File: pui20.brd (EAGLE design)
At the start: 160 x 100 mm, 0 parts

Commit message: + pui.sch (beginning)
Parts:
- added ANSCHLUSS1:X1: WANNENSTECKER-16, iceberg20:2X8
- added AUSGABE1:LED1, AUSGABE1:LED2: WS2812B, iceberg20:5050
- added AUSGABE1:LED10, AUSGABE1:LED3, AUSGABE1:LED4, AUSGABE1:LED5, AUSGABE1:LED6, AUSGABE1:LED7, AUSGABE1:LED8, AUSGABE1:LED9: LED-GREEN1, iceberg20:1206
- added AUSGABE1:R1, AUSGABE1:R2, AUSGABE1:R3, AUSGABE1:R4: 330, iceberg20:R0805
- added EINGABE1:S1, EINGABE1:S2, EINGABE1:S3, EINGABE1:S6: SMD-BUTTON, iceberg20:SWITCH-6MM-SMD
- added EINGABE1:S4, EINGABE1:S5: BUTTON-12MM, iceberg20:SWITCH-12MM-THT
- added EINGABE1:S7, EINGABE1:S8, EINGABE1:S9: TOGGLE-SWITCH, iceberg20:TOGGLE-SWITCH
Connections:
- new net +12V: ANSCHLUSS1:X1.1
- new net +5V: ANSCHLUSS1:X1.2
- new net ANSCHLUSS1:INTERRUPT: ANSCHLUSS1:X1.16
- new net ANSCHLUSS1:SCL: ANSCHLUSS1:X1.4
- new net ANSCHLUSS1:SDA: ANSCHLUSS1:X1.6
- new net AUSGABE1:+5V: AUSGABE1:LED1.VDD, AUSGABE1:LED2.VDD
- new net AUSGABE1:GND: AUSGABE1:LED1.GND, AUSGABE1:LED10.C, AUSGABE1:LED2.GND, AUSGABE1:LED6.C, AUSGABE1:LED7.C, AUSGABE1:LED8.C
- new net AUSGABE1:N$1: AUSGABE1:LED3.C, AUSGABE1:LED6.A
- new net AUSGABE1:N$11: AUSGABE1:LED9.A, AUSGABE1:R4.2
- new net AUSGABE1:N$12: AUSGABE1:LED10.A, AUSGABE1:LED9.C
- new net AUSGABE1:N$2: AUSGABE1:LED3.A, AUSGABE1:R1.2
- new net AUSGABE1:N$3: AUSGABE1:LED4.C, AUSGABE1:LED7.A
- new net AUSGABE1:N$4: AUSGABE1:LED5.C, AUSGABE1:LED8.A
- new net AUSGABE1:N$5: AUSGABE1:LED1.OUT, AUSGABE1:LED2.IN
- new net AUSGABE1:N$6: AUSGABE1:LED4.A, AUSGABE1:R2.2
- new net AUSGABE1:N$7: AUSGABE1:LED5.A, AUSGABE1:R3.2
- new net AUSGABE1:SHIFT-LED: AUSGABE1:R4.1
- new net EINGABE1:CALIBRATION-B: EINGABE1:S3.A1, EINGABE1:S3.A2
- new net EINGABE1:GND: EINGABE1:S1.B1, EINGABE1:S1.B2, EINGABE1:S2.B1, EINGABE1:S2.B2, EINGABE1:S3.B1, EINGABE1:S3.B2, EINGABE1:S4.3, EINGABE1:S5.3, EINGABE1:S6.B1, EINGABE1:S6.B2, EINGABE1:S7.C, EINGABE1:S8.C, EINGABE1:S9.C
- new net EINGABE1:KICK-B: EINGABE1:S2.A1, EINGABE1:S2.A2
- new net EINGABE1:SHIFT-B: EINGABE1:S6.A1, EINGABE1:S6.A2
- new net N$1: ANSCHLUSS1:X1.3, ANSCHLUSS1:X1.5, ANSCHLUSS1:X1.7
- new net N$2: ANSCHLUSS1:X1.8, EINGABE1:S4.1
- new net N$3: ANSCHLUSS1:X1.9, EINGABE1:S5.1
- new net N$4: ANSCHLUSS1:X1.15, EINGABE1:S1.A1, EINGABE1:S1.A2
- new net N$5: ANSCHLUSS1:X1.14, AUSGABE1:LED1.IN
- new net N$6: AUSGABE1:R3.1, EINGABE1:S9.A
- new net N$7: AUSGABE1:R1.1, EINGABE1:S7.A
- new net N$8: AUSGABE1:R2.1, EINGABE1:S8.A

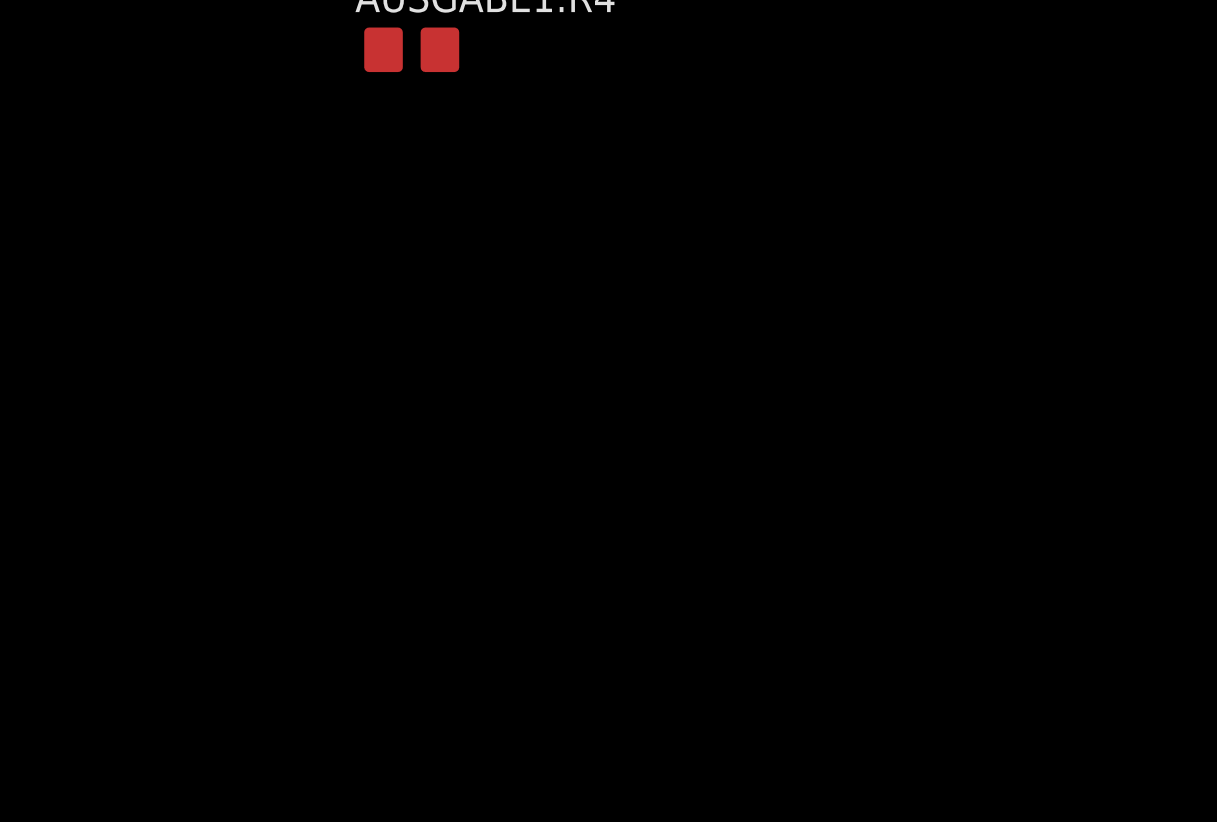
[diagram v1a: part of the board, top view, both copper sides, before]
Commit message: - pui.sch (Eingabe + Ausgabe)
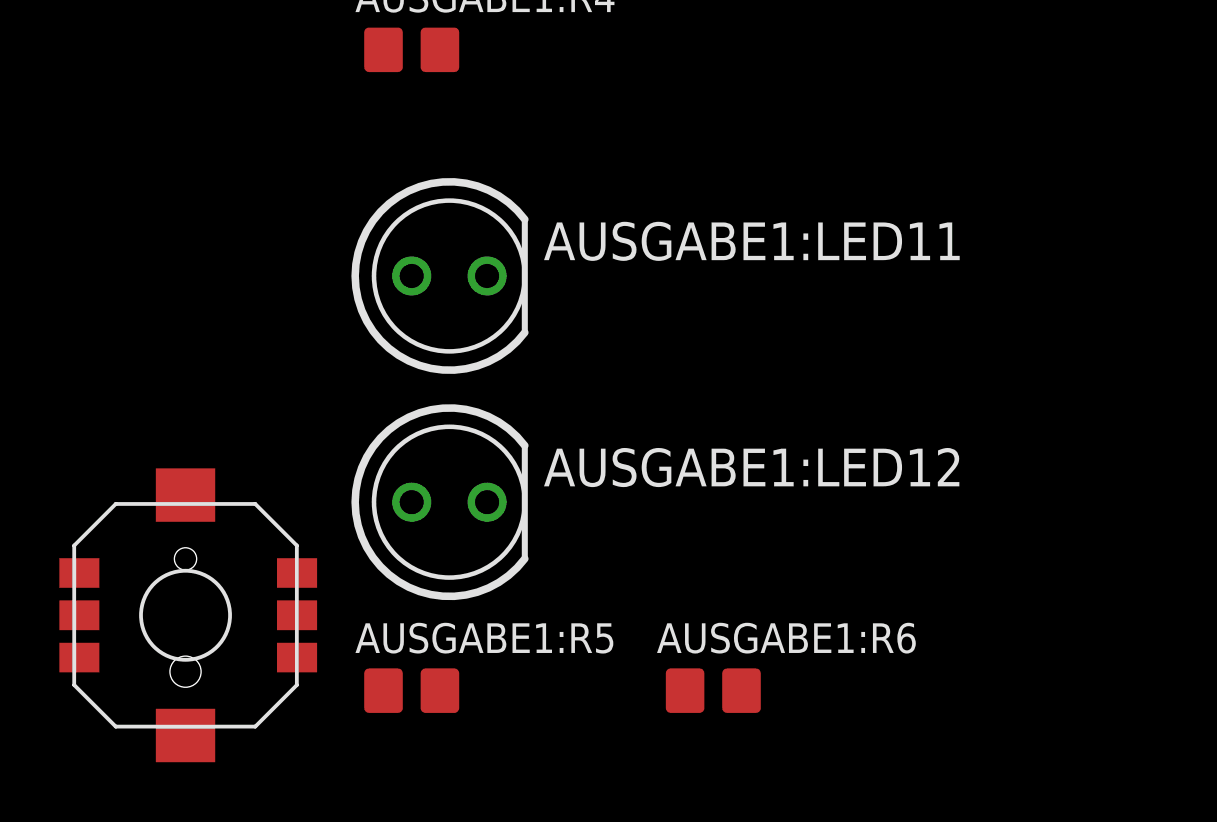
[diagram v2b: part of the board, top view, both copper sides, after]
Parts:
- added AUSGABE1:LED11, AUSGABE1:LED12: LED-GREEN-THT, iceberg20:LED_LED5MM
- added AUSGABE1:R5, AUSGABE1:R6: R, iceberg20:R0805
- added EINGABE1:U$1: JOYSTICK, iceberg20:SKRHAAE010
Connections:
- new net AUSGABE1:DEFENCE-LED: AUSGABE1:R6.1
- new net AUSGABE1:N$8: AUSGABE1:LED11.A, AUSGABE1:R5.2
- new net AUSGABE1:N$9: AUSGABE1:LED12.A, AUSGABE1:R6.2
- new net AUSGABE1:STRIKER-LED: AUSGABE1:R5.1
- new net EINGABE1:CENTER-J: EINGABE1:U$1.CENTER
- new net EINGABE1:DOWN-J: EINGABE1:U$1.C
- new net EINGABE1:LEFT-J: EINGABE1:U$1.A
- new net EINGABE1:RIGHT-J: EINGABE1:U$1.D
- new net EINGABE1:UP-J: EINGABE1:U$1.B
- net AUSGABE1:GND: now also AUSGABE1:LED11.K, AUSGABE1:LED12.K
- net EINGABE1:GND: now also EINGABE1:U$1.COMMON
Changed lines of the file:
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@@
 <attribute name="VALUE" x="-76.835" y="-106.68" size="1" layer="27" font="vector" ratio="20"/>
+</element>
+<element name="AUSGABE1:LED11" library="iceberg20" package="LED_LED5MM" value="LED-GREEN-THT" x="-73.66" y="-111.76" smashed="yes">
+<attribute name="BESTAND" value="" x="-73.66" y="-110.49" size="1.778" layer="27" display="off"/>
+<attribute name="HERSTELLER" value="" x="-73.66" y="-110.49" size="1.778" layer="27" display="off"/>
+<attribute name="HERSTELLER-NR" value="" x="-73.66" y="-110.49" size="1.778" layer="27" display="off"/>
+<attribute name="NAME" x="-70.485" y="-111.2266" size="1.27" layer="25" font="vector" ratio="20"/>
+<attribute name="SUPPLIER" value="" x="-73.66" y="-110.49" size="1.778" layer="27" display="off"/>
+<attribute name="SUPPLIER-NR" value="" x="-73.66" y="-110.49" size="1.778" layer="27" display="off"/>
+<attribute name="VALUE" x="-70.4596" y="-113.5634" size="1.27" layer="27" font="vector" ratio="20"/>
+</element>
+<element name="AUSGABE1:LED12" library="iceberg20" package="LED_LED5MM" value="LED-GREEN-THT" x="-73.66" y="-119.38" smashed="yes">
+<attribute name="BESTAND" value="" x="-73.66" y="-118.11" size="1.778" layer="27" display="off"/>
+<attribute name="HERSTELLER" value="" x="-73.66" y="-118.11" size="1.778" layer="27" display="off"/>
+<attribute name="HERSTELLER-NR" value="" x="-73.66" y="-118.11" size="1.778" layer="27" display="off"/>
+<attribute name="NAME" x="-70.485" y="-118.8466" size="1.27" layer="25" font="vector" ratio="20"/>
+<attribute name="SUPPLIER" value="" x="-73.66" y="-118.11" size="1.778" layer="27" display="off"/>
+<attribute name="SUPPLIER-NR" value="" x="-73.66" y="-118.11" size="1.778" layer="27" display="off"/>
+<attribute name="VALUE" x="-70.4596" y="-121.1834" size="1.27" layer="27" font="vector" ratio="20"/>
+</element>
+<element name="AUSGABE1:R5" library="iceberg20" package="R0805" package3d_urn="urn:adsk.eagle:package:23553/2" value="R" x="-74.93" y="-125.73" smashed="yes">
+<attribute name="BESTAND" value="-" x="-74.93" y="-124.46" size="1.778" layer="27" display="off"/>
+<attribute name="HERSTELLER" value="-" x="-74.93" y="-124.46" size="1.778" layer="27" display="off"/>
+<attribute name="HERSTELLER-NR" value="-" x="-74.93" y="-124.46" size="1.778" layer="27" display="off"/>
+<attribute name="NAME" x="-76.835" y="-124.46" size="1" layer="25" font="vector" ratio="20"/>
+<attribute name="SUPPLIER" value="-" x="-74.93" y="-124.46" size="1.778" layer="27" display="off"/>
+<attribute name="SUPPLIER-NR" value="-" x="-74.93" y="-124.46" size="1.778" layer="27" display="off"/>
+<attribute name="TOLERANZ" value="5%" x="-74.93" y="-124.46" size="1.778" layer="27" display="off"/>
+<attribute name="VALUE" x="-76.835" y="-128.27" size="1" layer="27" font="vector" ratio="20"/>
+</element>
+<element name="AUSGABE1:R6" library="iceberg20" package="R0805" package3d_urn="urn:adsk.eagle:package:23553/2" value="R" x="-64.77" y="-125.73" smashed="yes">
+<attribute name="BESTAND" value="-" x="-74.93" y="-130.81" size="1.778" layer="27" display="off"/>
+<attribute name="HERSTELLER" value="-" x="-74.93" y="-130.81" size="1.778" layer="27" display="off"/>
+<attribute name="HERSTELLER-NR" value="-" x="-74.93" y="-130.81" size="1.778" layer="27" display="off"/>
+<attribute name="NAME" x="-66.675" y="-124.46" size="1" layer="25" font="vector" ratio="20"/>
+<attribute name="SUPPLIER" value="-" x="-74.93" y="-130.81" size="1.778" layer="27" display="off"/>
+<attribute name="SUPPLIER-NR" value="-" x="-74.93" y="-130.81" size="1.778" layer="27" display="off"/>
+<attribute name="TOLERANZ" value="5%" x="-74.93" y="-130.81" size="1.778" layer="27" display="off"/>
+<attribute name="VALUE" x="-66.675" y="-128.27" size="1" layer="27" font="vector" ratio="20"/>
+</element>
+<element name="EINGABE1:U$1" library="iceberg20" package="SKRHAAE010" value="JOYSTICK" x="-82.55" y="-123.19" smashed="yes">
+<attribute name="BESTAND" value="0" x="-82.55" y="-123.19" size="1.778" layer="27" display="off"/>
+<attribute name="HERSTELLER" value="ALPS" x="-82.55" y="-123.19" size="1.778" layer="27" display="off"/>
+<attribute name="HERSTELLER-NR" value="SKRHAAE010 " x="-82.55" y="-123.19" size="1.778" layer="27" display="off"/>
+<attribute name="SUPPLIER" value="Mouser" x="-82.55" y="-123.19" size="1.778" layer="27" display="off"/>
+<attribute name="SUPPLIER-NR" value="688-SKRHAAE010 " x="-82.55" y="-123.19" size="1.778" layer="27" display="off"/>
 </element>
 </elements>
@@
 <contactref element="EINGABE1:S9" pad="C"/>
 <contactref element="EINGABE1:S8" pad="C"/>
+<contactref element="EINGABE1:U$1" pad="COMMON"/>
+<wire x1="5.08" y1="-80.01" x2="-78.793" y2="-123.19" width="0" layer="19" extent="1-1"/>
 <wire x1="5.08" y1="-76.2" x2="5.08" y2="-80.01" width="0" layer="19" extent="1-1"/>
 <wire x1="5.08" y1="-72.39" x2="5.08" y2="-76.2" width="0" layer="19" extent="1-1"/>
@@
 <contactref element="AUSGABE1:LED7" pad="C"/>
 <contactref element="AUSGABE1:LED10" pad="C"/>
+<contactref element="AUSGABE1:LED11" pad="K"/>
+<contactref element="AUSGABE1:LED12" pad="K"/>
+<wire x1="-72.39" y1="-111.76" x2="-72.39" y2="-119.38" width="0" layer="19" extent="1-1"/>
+<wire x1="-67.08" y1="-77.47" x2="-72.39" y2="-111.76" width="0" layer="19" extent="1-1"/>
 <wire x1="-60.73" y1="-77.47" x2="-67.08" y2="-77.47" width="0" layer="19" extent="1-1"/>
 <wire x1="-54.38" y1="-77.47" x2="-60.73" y2="-77.47" width="0" layer="19" extent="1-1"/>
@@
 <wire x1="2.54" y1="-76.2" x2="-75.88" y2="-91.44" width="0" layer="19" extent="1-1"/>
 </signal>
+<signal name="AUSGABE1:N$8">
+<contactref element="AUSGABE1:LED11" pad="A"/>
+<contactref element="AUSGABE1:R5" pad="2"/>
+<wire x1="-74.93" y1="-111.76" x2="-73.98" y2="-125.73" width="0" layer="19" extent="1-1"/>
+</signal>
+<signal name="AUSGABE1:N$9">
+<contactref element="AUSGABE1:LED12" pad="A"/>
+<contactref element="AUSGABE1:R6" pad="2"/>
+<wire x1="-63.82" y1="-125.73" x2="-74.93" y2="-119.38" width="0" layer="19" extent="1-1"/>
+</signal>
+<signal name="AUSGABE1:STRIKER-LED">
+<contactref element="AUSGABE1:R5" pad="1"/>
+</signal>
+<signal name="AUSGABE1:DEFENCE-LED">
+<contactref element="AUSGABE1:R6" pad="1"/>
+</signal>
+<signal name="EINGABE1:LEFT-J">
+<contactref element="EINGABE1:U$1" pad="A"/>
+</signal>
+<signal name="EINGABE1:CENTER-J">
+<contactref element="EINGABE1:U$1" pad="CENTER"/>
+</signal>
+<signal name="EINGABE1:DOWN-J">
+<contactref element="EINGABE1:U$1" pad="C"/>
+</signal>
+<signal name="EINGABE1:UP-J">
+<contactref element="EINGABE1:U$1" pad="B"/>
+</signal>
+<signal name="EINGABE1:RIGHT-J">
+<contactref element="EINGABE1:U$1" pad="D"/>
+</signal>
 </signals>

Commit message: + pui.brd (begin routing)
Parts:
- added EXPANDER1:C1: 200nF, iceberg20:C0805
- added EXPANDER1:IC1: GPIO-EXPANDER, iceberg20:DIL28-3
- added EXPANDER1:R1: 1k, iceberg20:R0805
- moved AUSGABE1:R6 214.9 mm to (70.5, 41.3), turned to 270 degrees
- moved EINGABE1:U$1 208.4 mm to (80.7, 6.36)
- moved AUSGABE1:R4 201.7 mm to (50.9, 53.4), turned to 90 degrees
- moved AUSGABE1:R5 196.1 mm to (31.7, 38.8), turned to 270 degrees
- moved AUSGABE1:R1 189.2 mm to (53.9, 53.4), turned to 90 degrees
- moved AUSGABE1:LED8 184.0 mm to (89.7, 16.3)
- moved AUSGABE1:R3 181.1 mm to (41.4, 40.9)
- moved AUSGABE1:LED7 180.5 mm to (89.5, 20.3)
- moved AUSGABE1:R2 180.1 mm to (39.9, 47.3)
- moved AUSGABE1:LED12 179.8 mm to (46.3, 14.5)
- moved AUSGABE1:LED6 177.1 mm to (89.4, 23.8)
- moved AUSGABE1:LED11 168.5 mm to (37.8, 14.6)
- moved AUSGABE1:LED5 163.0 mm to (83.8, 16.3)
- moved AUSGABE1:LED4 160.1 mm to (83.6, 20.3)
- moved AUSGABE1:LED3 157.2 mm to (83.5, 23.8)
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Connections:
- removed net ANSCHLUSS1:SCL: ANSCHLUSS1:X1.4
- removed net ANSCHLUSS1:SDA: ANSCHLUSS1:X1.6
- removed net AUSGABE1:+5V: AUSGABE1:LED1.VDD, AUSGABE1:LED2.VDD
- removed net AUSGABE1:DEFENCE-LED: AUSGABE1:R6.1
- removed net AUSGABE1:GND: AUSGABE1:LED1.GND, AUSGABE1:LED10.C, AUSGABE1:LED11.K, AUSGABE1:LED12.K, AUSGABE1:LED2.GND, AUSGABE1:LED6.C, AUSGABE1:LED7.C, AUSGABE1:LED8.C
- removed net AUSGABE1:SHIFT-LED: AUSGABE1:R4.1
- removed net AUSGABE1:STRIKER-LED: AUSGABE1:R5.1
- removed net EINGABE1:CALIBRATION-B: EINGABE1:S3.A1, EINGABE1:S3.A2
- removed net EINGABE1:CENTER-J: EINGABE1:U$1.CENTER
- removed net EINGABE1:DOWN-J: EINGABE1:U$1.C
- removed net EINGABE1:GND: EINGABE1:S1.B1, EINGABE1:S1.B2, EINGABE1:S2.B1, EINGABE1:S2.B2, EINGABE1:S3.B1, EINGABE1:S3.B2, EINGABE1:S4.3, EINGABE1:S5.3, EINGABE1:S6.B1, EINGABE1:S6.B2, EINGABE1:S7.C, EINGABE1:S8.C, EINGABE1:S9.C, EINGABE1:U$1.COMMON
- removed net EINGABE1:KICK-B: EINGABE1:S2.A1, EINGABE1:S2.A2
- removed net EINGABE1:LEFT-J: EINGABE1:U$1.A
- removed net EINGABE1:RIGHT-J: EINGABE1:U$1.D
- removed net EINGABE1:SHIFT-B: EINGABE1:S6.A1, EINGABE1:S6.A2
- removed net EINGABE1:UP-J: EINGABE1:U$1.B
- removed net N$8: AUSGABE1:R2.1, EINGABE1:S8.A
- new net EXPANDER1:A0: EXPANDER1:IC1.15
- new net EXPANDER1:A1: EXPANDER1:IC1.16
- new net EXPANDER1:A2: EXPANDER1:IC1.17
- new net EXPANDER1:GPA5: EXPANDER1:IC1.26
- new net EXPANDER1:GPA6: EXPANDER1:IC1.27
- new net EXPANDER1:GPA7: EXPANDER1:IC1.28
- new net EXPANDER1:INTA: EXPANDER1:IC1.20
- new net EXPANDER1:INTB: EXPANDER1:IC1.19
- new net EXPANDER1:NC: EXPANDER1:IC1.11
- new net EXPANDER1:RESET: EXPANDER1:IC1.18, EXPANDER1:R1.1
- new net GND: AUSGABE1:LED1.GND, AUSGABE1:LED10.C, AUSGABE1:LED11.K, AUSGABE1:LED12.K, AUSGABE1:LED2.GND, AUSGABE1:LED6.C, AUSGABE1:LED7.C, AUSGABE1:LED8.C, EINGABE1:S1.B1, EINGABE1:S1.B2, EINGABE1:S2.B1, EINGABE1:S2.B2, EINGABE1:S3.B1, EINGABE1:S3.B2, EINGABE1:S4.3, EINGABE1:S5.3, EINGABE1:S6.B1, EINGABE1:S6.B2, EINGABE1:S7.C, EINGABE1:S8.C, EINGABE1:S9.C, EINGABE1:U$1.COMMON, EXPANDER1:C1.2, EXPANDER1:IC1.10
- new net HEADSTART-LED: AUSGABE1:R1.1, EINGABE1:S7.A, EXPANDER1:IC1.21
- new net KICKER-LED: AUSGABE1:R3.1, EINGABE1:S9.A, EXPANDER1:IC1.23
- new net MOTOR-LED: AUSGABE1:R2.1, EINGABE1:S8.A, EXPANDER1:IC1.22
- new net N$11: EINGABE1:S3.A1, EINGABE1:S3.A2, EXPANDER1:IC1.3
- new net N$12: EINGABE1:U$1.CENTER, EXPANDER1:IC1.4
- new net N$13: EINGABE1:U$1.C, EXPANDER1:IC1.5
- new net N$14: EINGABE1:U$1.A, EXPANDER1:IC1.6
- new net N$15: EINGABE1:U$1.D, EXPANDER1:IC1.7
- new net N$16: EINGABE1:U$1.B, EXPANDER1:IC1.8
- new net N$9: EINGABE1:S2.A1, EINGABE1:S2.A2, EXPANDER1:IC1.2
- new net SCL: ANSCHLUSS1:X1.4, EXPANDER1:IC1.12
- new net SDA: ANSCHLUSS1:X1.6, EXPANDER1:IC1.13
- new net SHIFT-LED: AUSGABE1:R4.1, EINGABE1:S6.A1, EINGABE1:S6.A2, EXPANDER1:IC1.1
- net +5V: now also AUSGABE1:LED1.VDD, AUSGABE1:LED2.VDD, EXPANDER1:C1.1, EXPANDER1:IC1.9, EXPANDER1:R1.2
- net N$6: now also AUSGABE1:R6.1, EXPANDER1:IC1.24; no longer AUSGABE1:R3.1, EINGABE1:S9.A
- net N$7: now also AUSGABE1:R5.1, EXPANDER1:IC1.25; no longer AUSGABE1:R1.1, EINGABE1:S7.A
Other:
- board size 160 x 100 mm -> 95 x 30 mm

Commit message: - pui.brd (layout-update)
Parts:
- moved AUSGABE1:R2 51.8 mm to (82.0, 17.0)
- moved AUSGABE1:R4 49.3 mm to (33.0, 7.50), turned to 270 degrees
- moved AUSGABE1:R3 48.7 mm to (82.0, 14.0)
- moved EXPANDER1:R1 43.9 mm to (59.1, 8.50), turned to 270 degrees
- moved AUSGABE1:R1 43.7 mm to (82.0, 20.0), turned to 0 degrees
- moved AUSGABE1:LED1 41.5 mm to (26.5, 26.0)
- moved AUSGABE1:LED2 41.5 mm to (16.5, 26.0)
- moved ANSCHLUSS1:X1 32.1 mm to (86.0, 5.50), turned to 90 degrees
- moved EINGABE1:U$1 29.5 mm to (51.2, 5.86), turned to 45 degrees
- moved AUSGABE1:R6 26.4 mm to (49.0, 26.0)
- moved EXPANDER1:C1 16.9 mm to (55.5, 26.0)
- moved AUSGABE1:R5 15.0 mm to (39.5, 26.0)
- moved AUSGABE1:LED11 11.7 mm to (35.0, 26.0), turned to 180 degrees
- moved AUSGABE1:LED12 11.6 mm to (44.5, 26.0), turned to 180 degrees
- moved EXPANDER1:IC1 7.16 mm to (50.2, 16.8)
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
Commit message: - pui.brd (Layout + Routing)
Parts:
- moved ANSCHLUSS1:X1 61.2 mm to (28.0, 25.0)
- moved AUSGABE1:LED1 57.6 mm to (83.5, 18.0)
- moved AUSGABE1:LED2 57.1 mm to (73.0, 18.0)
- moved AUSGABE1:LED11 48.5 mm to (83.5, 26.0), turned to 0 degrees
- moved AUSGABE1:R5 39.0 mm to (78.5, 26.0), turned to 90 degrees
- moved EINGABE1:S7 37.1 mm to (38.5, 26.5)
- moved EINGABE1:S8 37.0 mm to (38.5, 23.0)
- moved EINGABE1:S9 36.9 mm to (38.5, 19.5)
- moved AUSGABE1:R1 36.1 mm to (46.5, 26.5)
- moved AUSGABE1:R2 36.0 mm to (46.5, 23.0)
- moved AUSGABE1:R3 35.9 mm to (46.5, 19.5)
- moved AUSGABE1:LED3 35.6 mm to (51.5, 26.5)
- moved AUSGABE1:LED4 35.5 mm to (51.5, 23.0)
- moved AUSGABE1:LED5 35.4 mm to (51.5, 19.5)
- moved AUSGABE1:LED6 35.1 mm to (57.0, 26.5)
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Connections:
- net HEADSTART-LED: now also EXPANDER1:IC1.23; no longer EXPANDER1:IC1.21
- net KICKER-LED: now also EXPANDER1:IC1.21; no longer EXPANDER1:IC1.23
- net N$12: now also EINGABE1:U$1.A; no longer EINGABE1:U$1.CENTER
- net N$13: now also EINGABE1:U$1.CENTER; no longer EINGABE1:U$1.C
- net N$14: now also EINGABE1:U$1.C; no longer EINGABE1:U$1.A
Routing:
- net N$9: track 0.00 -> 82.3 mm, vias 0 -> 2
- net N$5: track 0.00 -> 80.9 mm
- net N$11: track 0.00 -> 68.1 mm
- net SHIFT-LED: track 0.00 -> 65.3 mm
- net N$12: track 0.00 -> 43.7 mm
- net HEADSTART-LED: track 0.00 -> 43.2 mm
- net N$13: track 0.00 -> 38.9 mm
- net MOTOR-LED: track 0.00 -> 38.9 mm
- net KICKER-LED: track 0.00 -> 34.9 mm
- net GND: track 0.00 -> 32.4 mm, vias 0 -> 14
- net N$14: track 0.00 -> 32.2 mm
- net N$17: track 0.00 -> 32.0 mm
- net N$10: track 0.00 -> 32.0 mm
- net N$8: track 0.00 -> 31.0 mm
- net N$2: track 0.00 -> 29.9 mm
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- added copper zone on layer 16, net GND
